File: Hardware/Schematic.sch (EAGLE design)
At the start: 105 parts, among them IC1 BQ25180YBGR, IC3 BMA421, IC4 DRV2605YZFR, IC9 RT6160AWSC_RT6160AWSC, J1 503480-2400, J2 TC2030-IDC, J4 KH-TYPE-C-16P, Q1 20V/4.2A/52mΩ/1.4W, Q3 SI1308EDL-T1-GE3, SW1 2025-10-22_07-23-44_LIBRARY_E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, SW2 2025-10-22_07-23-44_LIBRARY_E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, SW3 2025-10-22_07-23-44_LIBRARY_E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, U1 NRF52840_QF, U3 MAX17048G+T10, X1 32MHz

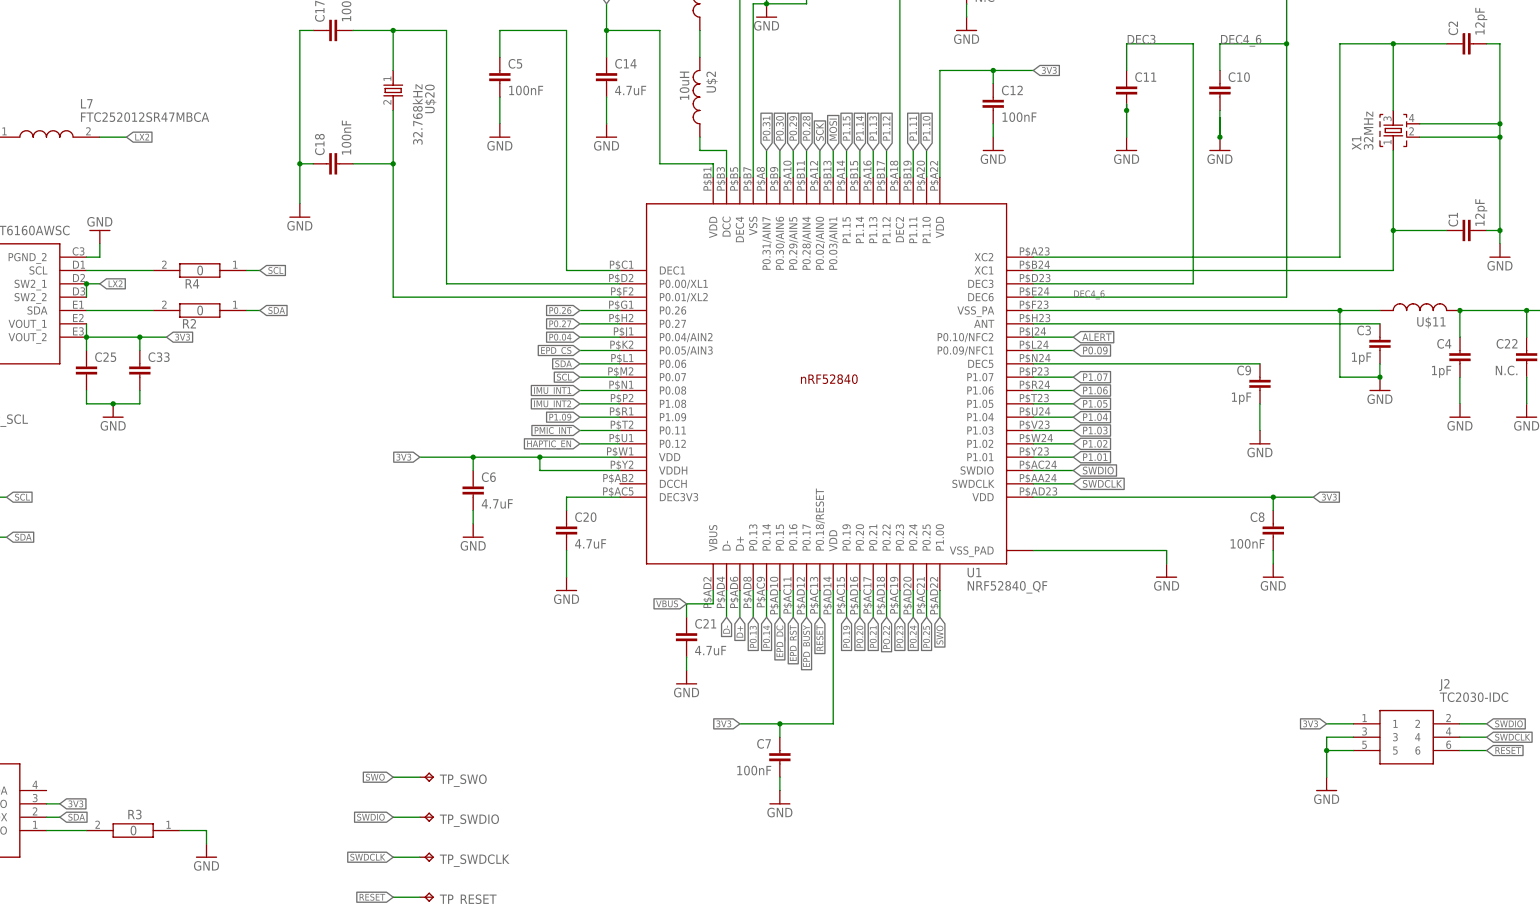
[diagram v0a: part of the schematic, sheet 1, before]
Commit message: Add modified files: Schematic, PCB_2d, PCB_3d in .f3d format(Fusion crashes at .step export), exploded_view in .f3z format(same problem), bill.bom, gerbers.zip, pick.cpl.
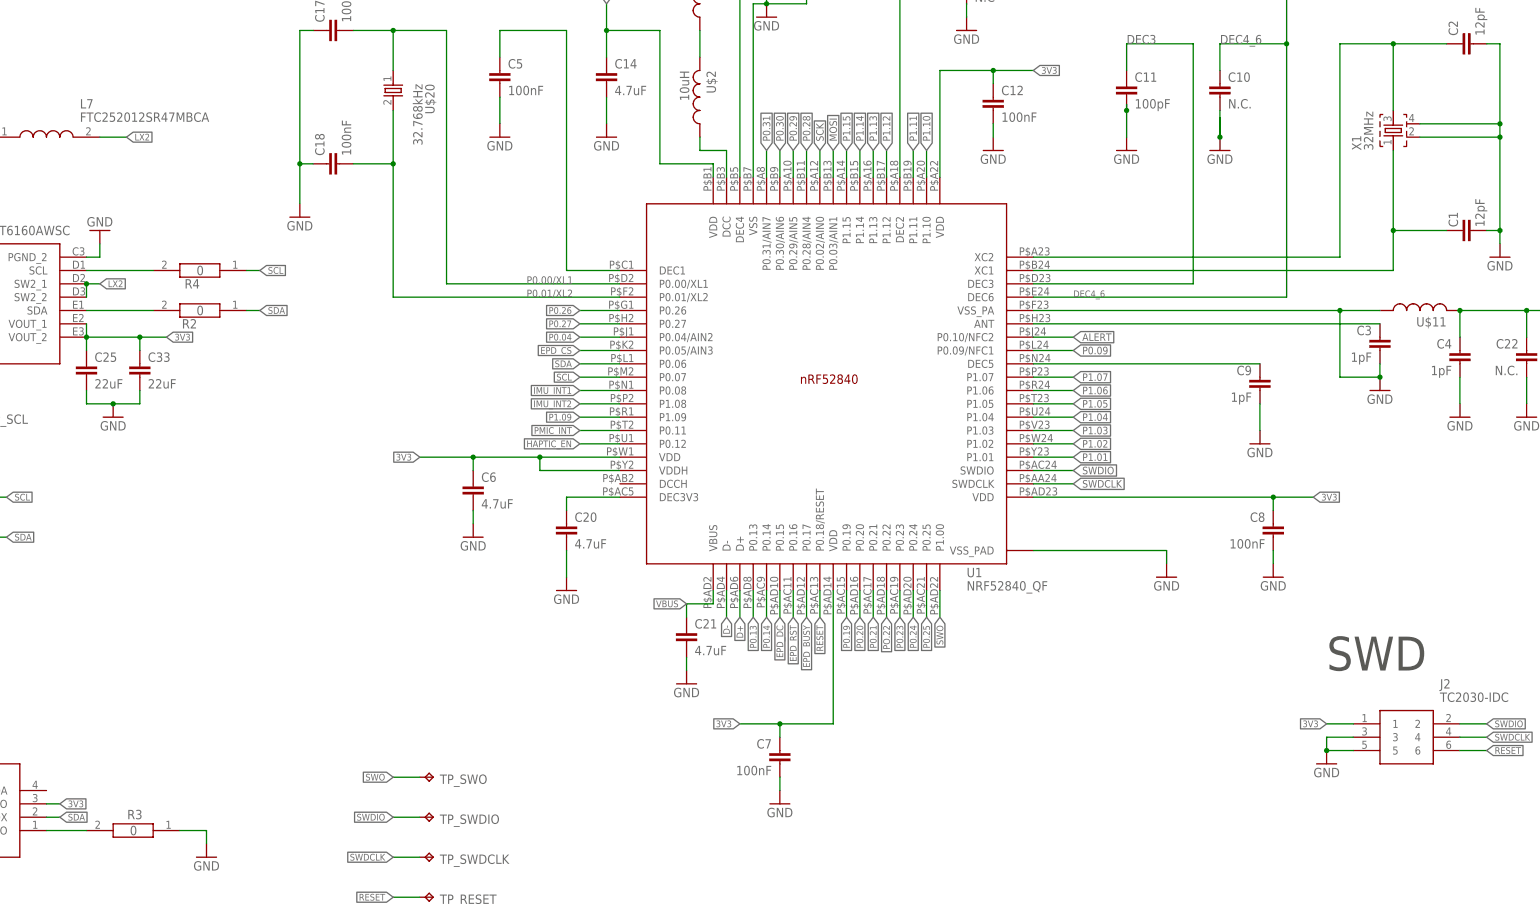
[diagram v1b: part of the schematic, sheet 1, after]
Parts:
- C10: value (none) -> N.C.
- C11: value (none) -> 100pF
- C25, C33: value (none) -> 22uF
- C43: value (none) -> 4.7uF
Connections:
- net N$59 renamed P0.01/XL2
- net N$75 renamed P0.00/XL1
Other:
- note added: "SWD"
